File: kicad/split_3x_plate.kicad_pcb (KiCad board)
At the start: 2 copper layers, 121.4 x 121.2 mm, 6 parts

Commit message: changed the plate to have copper pane, updated gerbers of pcb and plate
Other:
- board text added: "DracuLad by MangoIV"
- board text removed: "DracuLad XXXII by MangoIV"

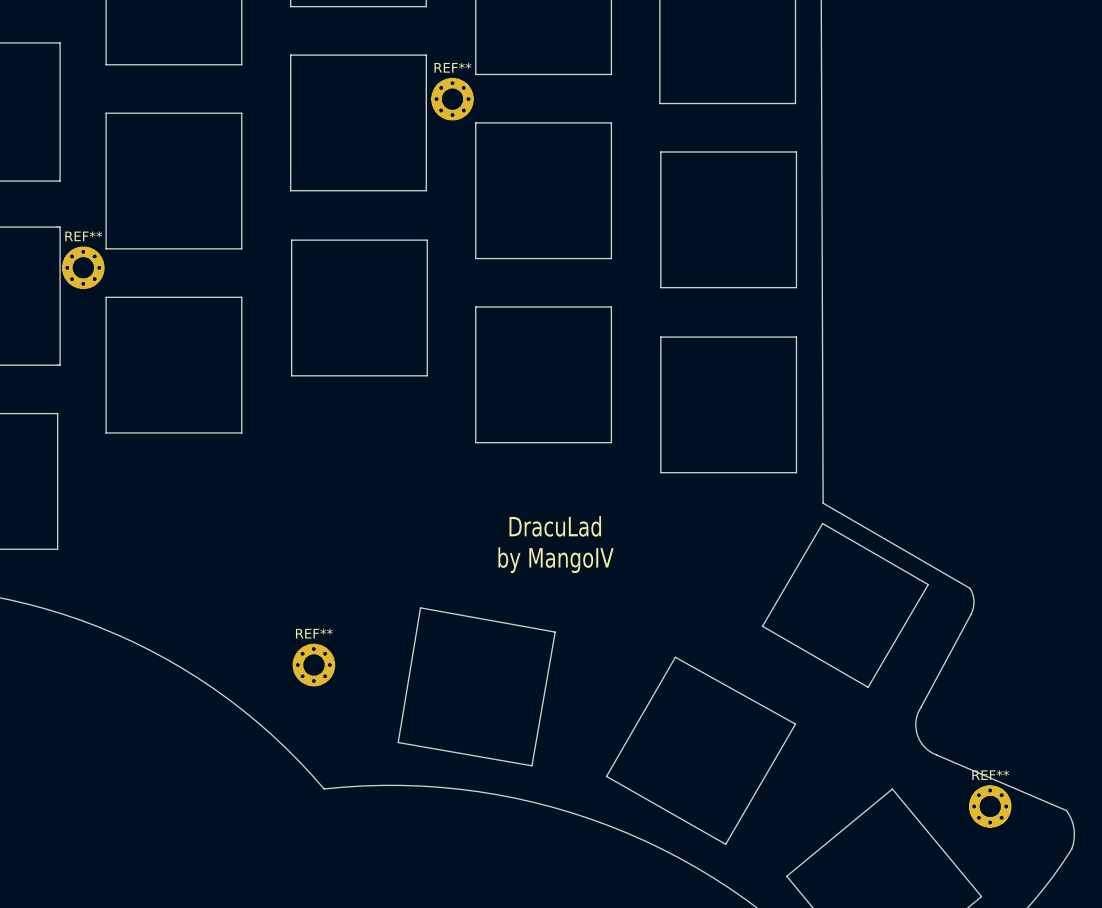
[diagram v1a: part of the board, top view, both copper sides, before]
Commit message: added support for the pimoroni trackball breakout, changed a bunch of things, rewired the pcb, changed the bottom plate to be prettier, added some silkscreen, changed the position of one of the mounting holes, changed the angle of the trrs jacks to be properly aligned, changed the top plate to look better
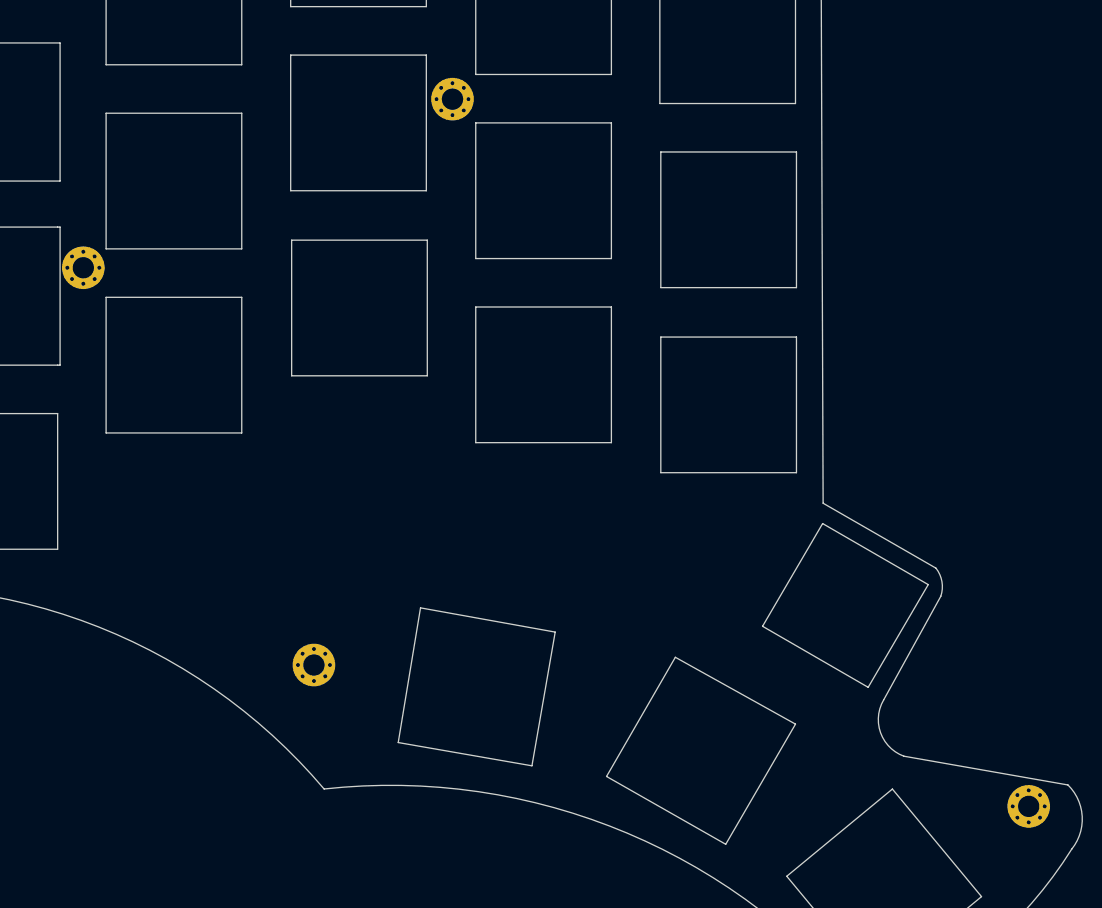
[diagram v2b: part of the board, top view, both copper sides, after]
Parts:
-  : renamed from REF** (x4)
- moved   3.97 mm to (194.5, 141.3)
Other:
- board size 121.4 x 121.2 mm -> 122.2 x 121.2 mm
- board text removed: "DracuLad by MangoIV"
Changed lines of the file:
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@@
   (general
     (thickness 1.6)
-    (drawings 92)
+    (drawings 90)
     (tracks 0)
     (zones 0)
@@
     (tags "mounting hole 2.2mm m2")
     (attr virtual)
-    (fp_text reference REF** (at 0 -3.2) (layer F.SilkS)
+    (fp_text reference " " (at 0 -3.2) (layer F.SilkS)
       (effects (font (size 1 1) (thickness 0.15)))
     )
@@
     (tags "mounting hole 2.2mm m2")
     (attr virtual)
-    (fp_text reference REF** (at 0 -3.2) (layer F.SilkS)
+    (fp_text reference " " (at 0 -3.2) (layer F.SilkS)
       (effects (font (size 1 1) (thickness 0.15)))
     )
@@
     (tags "mounting hole 2.2mm m2")
     (attr virtual)
-    (fp_text reference REF** (at 0 -3.2) (layer F.SilkS)
+    (fp_text reference " " (at 0 -3.2) (layer F.SilkS)
       (effects (font (size 1 1) (thickness 0.15)))
     )
@@
   )
   (module MountingHole:MountingHole_2.2mm_M2_Pad_Via (layer F.Cu)
-    (at 190.5 141.3)
+    (at 194.46875 141.2875)
     (descr "Mounting Hole 2.2mm, M2")
     (tags "mounting hole 2.2mm m2")
     (attr virtual)
-    (fp_text reference REF** (at 0 -3.2) (layer F.SilkS)
+    (fp_text reference " " (at 0 -3.2) (layer F.SilkS)
       (effects (font (size 1 1) (thickness 0.15)))
     )
@@
       (xy -3.664033 -5.1054) (xy -3.627864 -5.093332)) (layer F.Mask) (width 0.01))
   )
-  (gr_text "DracuLad\nby MangoIV" (at 145.3 114.1) (layer B.SilkS)
-    (effects (font (size 2 1.5) (thickness 0.2)) (justify mirror))
-  )
-  (gr_text "DracuLad\nby MangoIV" (at 145.6 114.1) (layer F.SilkS)
-    (effects (font (size 2 1.5) (thickness 0.2)))
-  )
+  (gr_arc (start 182.959325 132.335877) (end 179.5 130.3) (angle -100.4996841) (layer Edge.Cuts) (width 0.05))
+  (gr_line (start 198.521567 139.078078) (end 181.58793 136.108277) (layer Edge.Cuts) (width 0.05))
   (gr_line (start 169.5 148.5) (end 180.4 139.5) (layer Edge.Cuts) (width 0.05))
   (gr_line (start 169.5 148.5) (end 178.7 159.6) (layer Edge.Cuts) (width 0.05))
   (gr_line (start 178.7 159.6) (end 189.6 150.6) (layer Edge.Cuts) (width 0.05))
   (gr_line (start 180.4 139.5) (end 189.6 150.6) (layer Edge.Cuts) (width 0.05))
-  (gr_arc (start 195 144.2) (end 198.906839 145.704287) (angle -57.31252182) (layer Edge.Cuts) (width 0.05))
+  (gr_arc (start 195.052625 142.60408) (end 198.906839 145.704287) (angle -84.27945884) (layer Edge.Cuts) (width 0.05))
   (gr_line (start 163.2 145.2) (end 150.9 138.2) (layer Edge.Cuts) (width 0.05))
   (gr_line (start 158 125.9) (end 150.9 138.2) (layer Edge.Cuts) (width 0.05))
@@
   (gr_line (start 94.5 62.5) (end 94.5 76.75) (layer Edge.Cuts) (width 0.05))
   (gr_line (start 80.25 62.5) (end 94.5 62.5) (layer Edge.Cuts) (width 0.05))
-  (gr_arc (start 186.082706 120.213242) (end 188.5 121.5) (angle -59.21442654) (layer Edge.Cuts) (width 0.05))
-  (gr_line (start 173.25 110) (end 188.425381 118.795169) (layer Edge.Cuts) (width 0.05))
+  (gr_arc (start 182.457325 118.618073) (end 185.4 119.6) (angle -56.59332546) (layer Edge.Cuts) (width 0.05))
+  (gr_line (start 173.25 110) (end 184.897194 116.702203) (layer Edge.Cuts) (width 0.05))
   (gr_line (start 173.037499 51.593751) (end 173.25 110) (layer Edge.Cuts) (width 0.05))
-  (gr_line (start 183.378307 131.022441) (end 188.5 121.5) (layer Edge.Cuts) (width 0.05))
-  (gr_arc (start 186.135252 132.87718) (end 183.378307 131.022441) (angle -103.9528162) (layer Edge.Cuts) (width 0.05))
-  (gr_line (start 198.375965 141.724291) (end 185 136) (layer Edge.Cuts) (width 0.05))
+  (gr_line (start 179.5 130.3) (end 185.4 119.6) (layer Edge.Cuts) (width 0.05))
   (gr_arc (start 76.786648 177.505299) (end 121.749255 139.493235) (angle -48.80720594) (layer Edge.Cuts) (width 0.05))
   (gr_arc (start 128.62912 201.939184) (end 178.128606 163.252882) (angle -58.27770953) (layer Edge.Cuts) (width 0.05))

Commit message: generated gerbers for the second run
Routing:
- added copper zone on B.Cu, net (none)
- added copper zone on F.Cu, net (none)
